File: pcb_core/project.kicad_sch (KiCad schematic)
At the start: 35 parts, among them J1 PCBConnector, J2 1725656, J20 PCBConnector, J21 PCBConnector, J22 PCBConnector, J25 PCBConnector, J27 PCBConnector, T1 Tab, T2 Tab, T3 Tab, T4 Tab, T5 Tab, T6 Tab, T7 Tab, T8 Tab

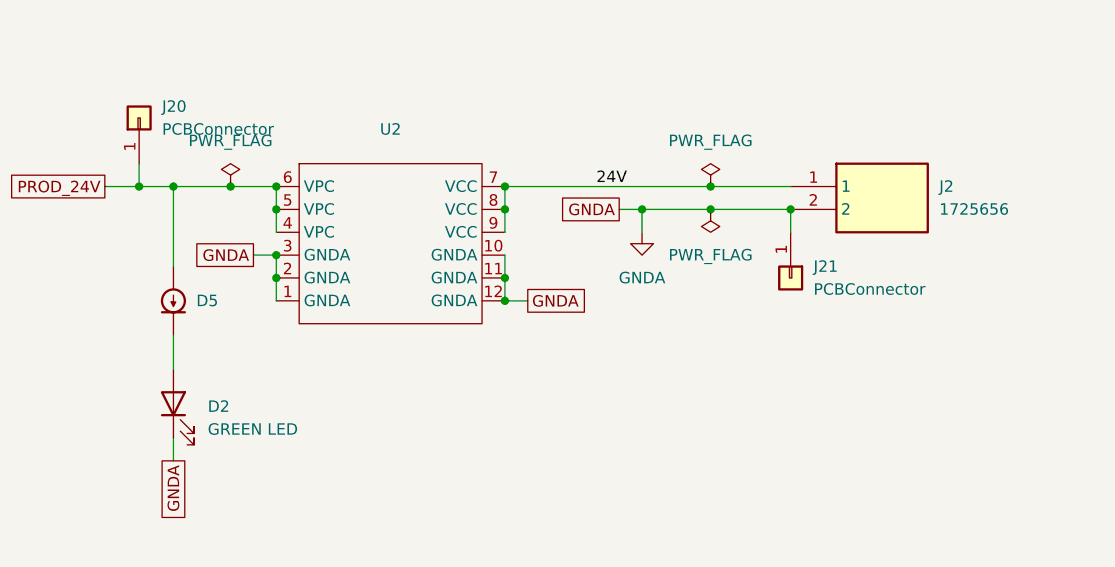
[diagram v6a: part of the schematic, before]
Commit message: Add ESP32Dev PCB
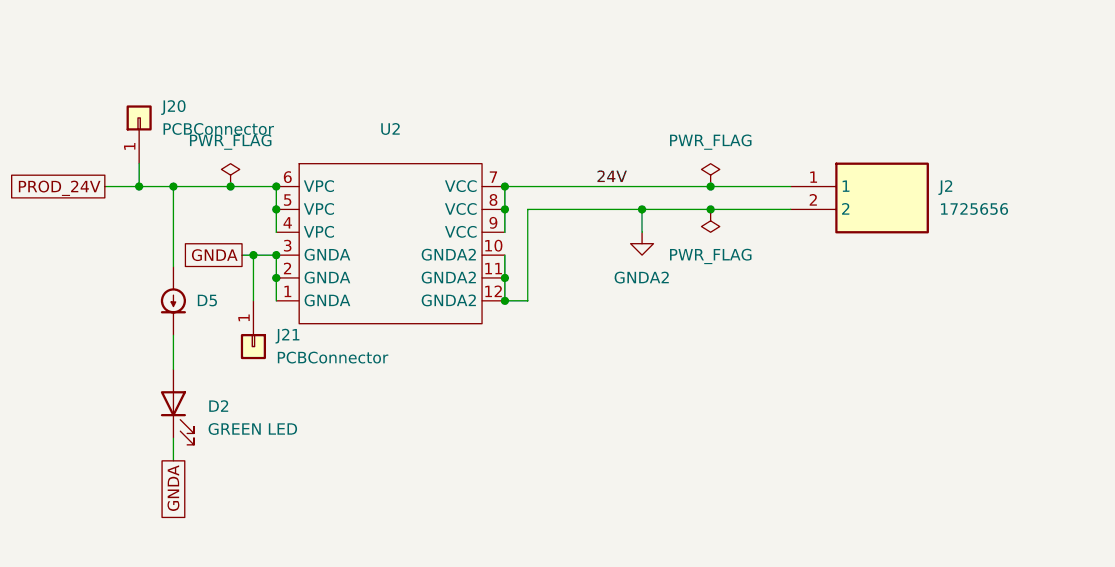
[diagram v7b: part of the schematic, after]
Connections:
- net GNDA: no longer J2.2, U2.10 (GNDA), U2.11 (GNDA), U2.12 (GNDA)
- new net GNDA2: J2.2, U2.10 (GNDA2), U2.11 (GNDA2), U2.12 (GNDA2)
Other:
- moved on the sheet: J21
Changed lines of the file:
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@@
 	)
 	(junction
-		(at 328.93 130.81)
-		(diameter 0)
-		(color 0 0 0 0)
-	)
-	(junction
 		(at 276.86 62.23)
 		(diameter 0)
@@
 	)
 	(junction
+		(at 269.24 135.89)
+		(diameter 0)
+		(color 0 0 0 0)
+	)
+	(junction
 		(at 280.67 187.96)
 		(diameter 0)
@@
 	(wire
 		(pts
+			(xy 299.72 140.97) (xy 299.72 130.81)
+		)
+		(stroke
+			(width 0)
+			(type default)
+		)
+	)
+	(wire
+		(pts
 			(xy 41.91 109.22) (xy 44.45 109.22)
 		)
@@
 	(wire
 		(pts
+			(xy 269.24 135.89) (xy 271.78 135.89)
+		)
+		(stroke
+			(width 0)
+			(type default)
+		)
+	)
+	(wire
+		(pts
 			(xy 135.89 101.6) (xy 138.43 101.6)
 		)
@@
 	(wire
 		(pts
-			(xy 269.24 135.89) (xy 271.78 135.89)
+			(xy 267.97 135.89) (xy 269.24 135.89)
 		)
 		(stroke
@@
 	(wire
 		(pts
-			(xy 309.88 130.81) (xy 312.42 130.81)
+			(xy 299.72 130.81) (xy 312.42 130.81)
 		)
 		(stroke
@@
 	(wire
 		(pts
+			(xy 269.24 135.89) (xy 269.24 140.97)
+		)
+		(stroke
+			(width 0)
+			(type default)
+		)
+	)
+	(wire
+		(pts
 			(xy 260.35 128.27) (xy 266.7 128.27)
 		)
@@
 	(wire
 		(pts
-			(xy 328.93 130.81) (xy 328.93 133.35)
-		)
-		(stroke
-			(width 0)
-			(type default)
-		)
-	)
-	(wire
-		(pts
 			(xy 40.64 48.26) (xy 43.18 48.26)
 		)
@@
 	(global_label "GNDA"
 		(shape passive)
-		(at 269.24 135.89 180)
+		(at 267.97 135.89 180)
 		(fields_autoplaced yes)
 		(effects
@@
 		)
 		(property "Intersheetrefs" "${INTERSHEET_REFS}"
-			(at 262.407 135.89 0)
+			(at 261.137 135.89 0)
 			(effects
 				(font
@@
 		)
 	)
-	(global_label "GNDA"
-		(shape passive)
-		(at 309.88 130.81 180)
-		(fields_autoplaced yes)
-		(effects
-			(font
-				(size 1.27 1.27)
-			)
-			(justify right)
-		)
-		(property "Intersheetrefs" "${INTERSHEET_REFS}"
-			(at 303.047 130.81 0)
-			(effects
-				(font
-					(size 1.27 1.27)
-				)
-				(justify right)
-				(hide yes)
-			)
-		)
-	)
 	(global_label "GNDD"
 		(shape passive)
@@
 		)
 	)
-	(global_label "GNDA"
-		(shape passive)
-		(at 299.72 140.97 0)
-		(fields_autoplaced yes)
-		(effects
-			(font
-				(size 1.27 1.27)
-			)
-			(justify left)
-		)
-		(property "Intersheetrefs" "${INTERSHEET_REFS}"
-			(at 306.553 140.97 0)
-			(effects
-				(font
-					(size 1.27 1.27)
-				)
-				(justify left)
-				(hide yes)
-			)
-		)
-	)
 	(global_label "IN1_4"
 		(shape input)
@@
 			)
 		)
-		(property "Value" "GNDA"
+		(property "Value" "GNDA2"
 			(at 312.42 138.43 0)
 			(effects
@@
 	(symbol
 		(lib_id "Connector_Generic:Conn_01x01")
-		(at 328.93 138.43 270)
+		(at 269.24 146.05 270)
 		(unit 1)
 		(exclude_from_sim no)
@@
 		(fields_autoplaced yes)
 		(property "Reference" "J21"
-			(at 331.47 137.1599 90)
+			(at 271.78 144.7799 90)
 			(effects
 				(font
@@
 		)
 		(property "Value" "PCBConnector"
-			(at 331.47 139.6999 90)
+			(at 271.78 147.3199 90)
 			(effects
 				(font
@@
 		)
 		(property "Footprint" "TestPoint:TestPoint_THTPad_D3.0mm_Drill1.5mm"
-			(at 328.93 138.43 0)
+			(at 269.24 146.05 0)
 			(effects
 				(font
@@
 		)
 		(property "Datasheet" "~"
-			(at 328.93 138.43 0)
+			(at 269.24 146.05 0)
 			(effects
 				(font
@@
 		)
 		(property "Description" ""
-			(at 328.93 138.43 0)
+			(at 269.24 146.05 0)
 			(effects
 				(font
@@
 		)
 		(property "Config" ""
-			(at 328.93 138.43 0)
+			(at 269.24 146.05 0)
 			(effects
 				(font
@@
 		)
 		(property "LCSC# Alt1" ""
-			(at 328.93 138.43 0)
+			(at 269.24 146.05 0)
 			(effects
 				(font
@@
 		)
 		(property "AISLER_MPN" ""
-			(at 328.93 138.43 0)
+			(at 269.24 146.05 0)
 			(effects
 				(font
@@
 		)
 		(property "Mouser# Alt1" ""
-			(at 328.93 138.43 0)
+			(at 269.24 146.05 0)
 			(effects
 				(font
